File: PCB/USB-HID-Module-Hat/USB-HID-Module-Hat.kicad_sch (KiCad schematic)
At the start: 21 parts, among them J1 RJHSE-5381, J2 Raspberry_Pi_2_3, U1 MAX3535ECWI+T

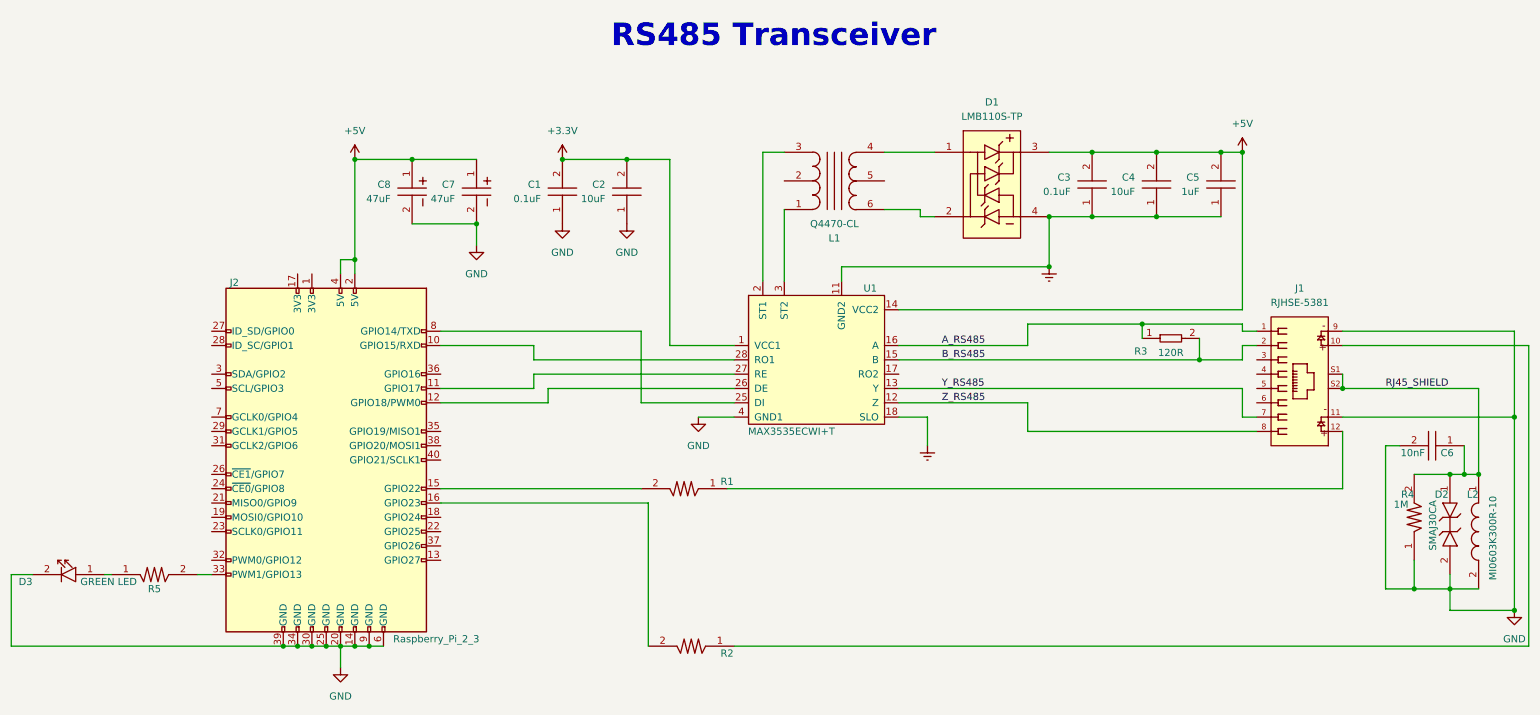
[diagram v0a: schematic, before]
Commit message: Revised Scheamtic
Added schematic pages and added power schematic
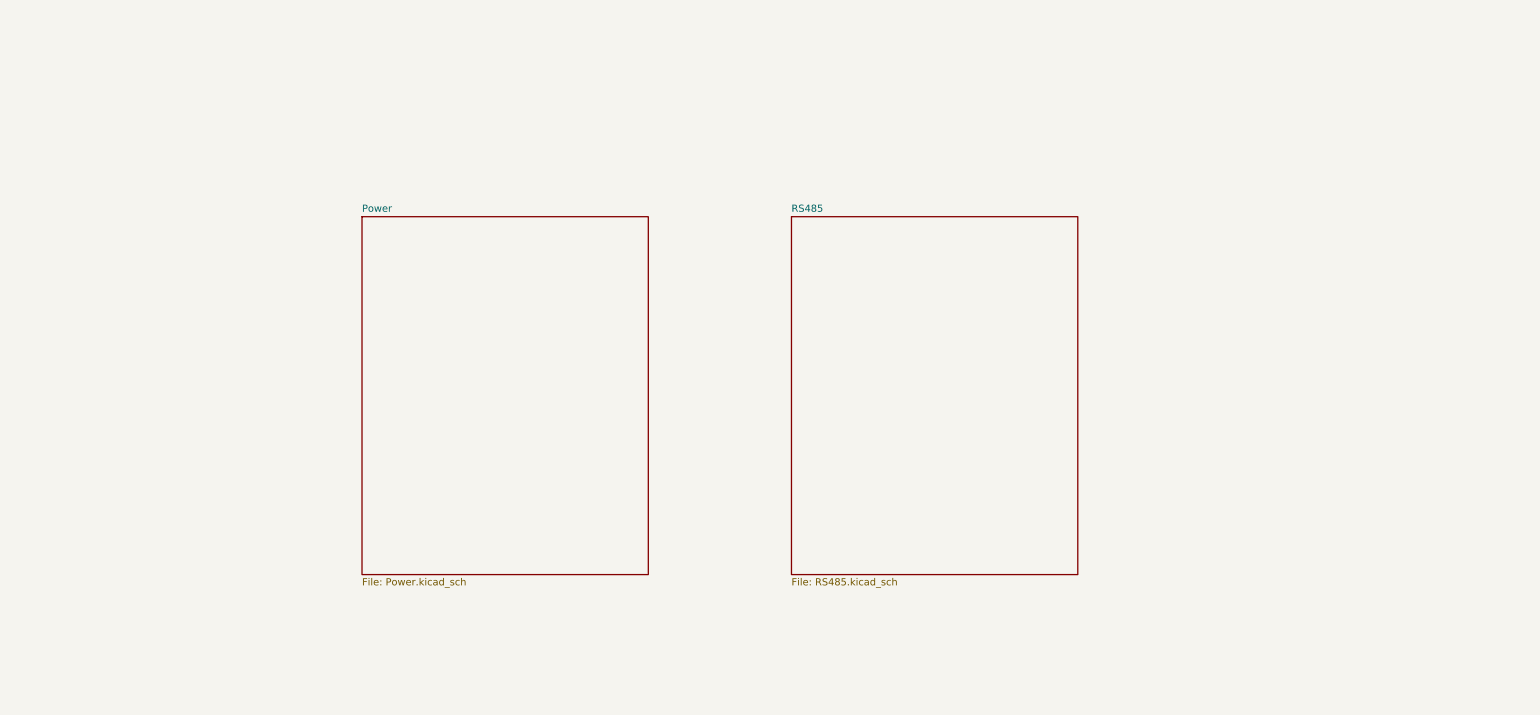
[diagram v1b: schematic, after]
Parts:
- removed C1, C3: CL10B104JB8NNNC, AVR-KiCAD-Lib-Capacitors:C0603, symbol AVR-KiCAD-Lib-Capacitors:CL10B104JB8NNNC
- removed C2, C4: CGA5L3X5R1V106K160AB, AVR-KiCAD-Lib-Capacitors:C1206, symbol AVR-KiCAD-Lib-Capacitors:CGA5L3X5R1V106K160AB
- removed C5: C1206C105K3RACAUTO, AVR-KiCAD-Lib-Diodes:D_SOD-123, symbol AVR-KiCAD-Lib-Capacitors:C1206C105K3RACAUTO
- removed C6: C0805C103KCRACAUTO, AVR-KiCAD-Lib-Capacitors:C0805, symbol AVR-KiCAD-Lib-Capacitors:C0805C103KCRACAUTO
- removed C7, C8: UCM1C470MCL1GS, AVR-KiCAD-Lib-Capacitors:UCM1C470MCL1GS, symbol AVR-KiCAD-Lib-Capacitors:UCM1C470MCL1GS
- removed D1: LMB110S-TP, AVR-KiCAD-Lib-Diodes:LMB110S-TP, symbol AVR-KiCAD-Lib-Diodes:LMB110S-TP
- removed D2: SMAJ30CA, AVR-KiCAD-Lib-Diodes:SMAJ30CA, symbol AVR-KiCAD-Lib-Diodes:SMAJ30CA
- removed D3: LTST-C194KGKT, AVR-KiCAD-Lib-Diodes:LED0603, symbol AVR-KiCAD-Lib-Diodes:LTST-C194KGKT
- removed J1: RJHSE-5381, AVR-KiCAD-Lib-Connectors:AMPHENOL_RJHSE-5381, symbol AVR-KiCAD-Lib-Connectors:RJHSE-5381
- removed J2: Raspberry_Pi_2_3, AVR-KiCAD-Lib-Connectors:SULLINS_PPPC202LFBN-RC_RPi5, symbol Connector:Raspberry_Pi_2_3
- removed L1: Q4470-CL, AVR-KiCAD-Lib-Transformers:SO6_Q4470-CL_C-SIZE_COC, symbol AVR-KiCAD-Lib-Transformers:Q4470-CL
- removed L2: MI0603K300R-10, AVR-KiCAD-Lib-Inductors:MI0603K300R-10, symbol AVR-KiCAD-Lib-Inductors:MI0603K300R-10
- removed R1, R2, R5: RC0603FR-07470RL, AVR-KiCAD-Lib-Resistors:R0603, symbol AVR-KiCAD-Lib-Resistors:RC0603FR-07470RL
- removed R3: AC0402FR-07120RL, AVR-KiCAD-Lib-Resistors:R0402, symbol AVR-KiCAD-Lib-Resistors:AC0402FR-07120RL
- removed R4: RC1206FR-071ML, AVR-KiCAD-Lib-Resistors:R1206, symbol AVR-KiCAD-Lib-Resistors:RC1206FR-071ML
- removed U1: MAX3535ECWI+T, AVR-KiCAD-Lib-ICs:21-0145_W28M&plus_9_MXM, symbol AVR-KiCAD-Lib-ICs:MAX3535ECWI+T
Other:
- added sheet Power (Power.kicad_sch)
- added sheet RS485 (RS485.kicad_sch)
- note removed: "RS485 Transceiver"
